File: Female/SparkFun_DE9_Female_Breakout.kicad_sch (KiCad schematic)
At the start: 9 parts, among them J2 Conn_01x09, J3 Conn_01x01, J4 Conn_01x01, J5 DB9-Female

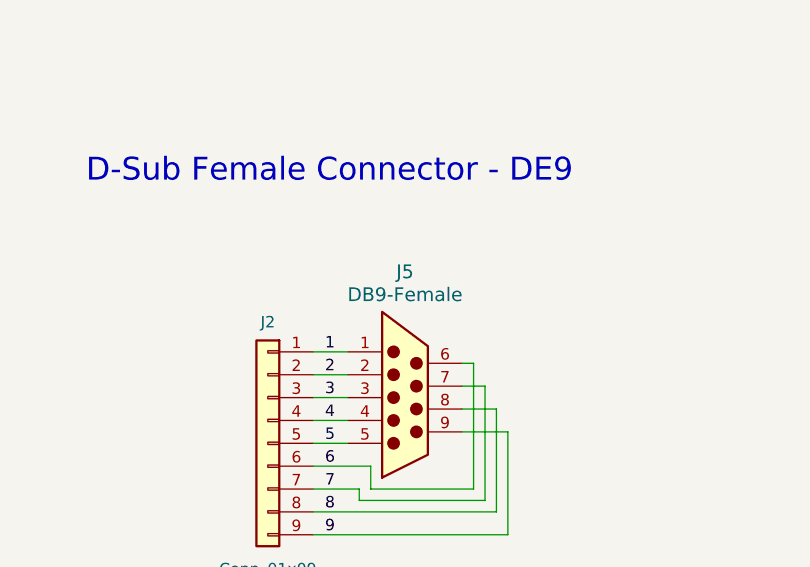
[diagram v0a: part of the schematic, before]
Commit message: Updates symbol, footprint, and design with the new renamed parts
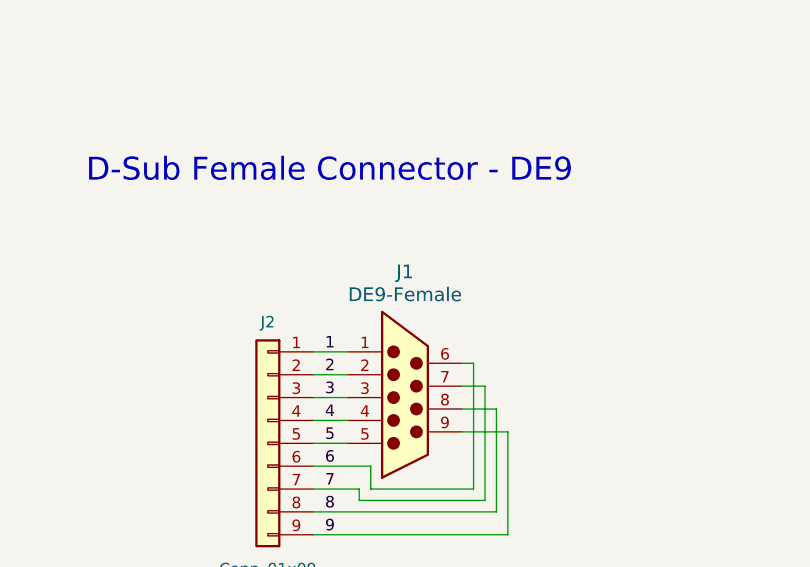
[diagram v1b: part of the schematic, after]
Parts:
- removed J5: DB9-Female, DE9_Footprint:DB9_Female, symbol DB9-Female:DB9 Female
- added J1: DE9-Female, DE9-Footprints:DE9_Female, symbol DE9-Female:DE9 Female
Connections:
- net 1: now also J1.1
- net 2: now also J1.2
- net 3: now also J1.3
- net 4: now also J1.4
- net 5: now also J1.5
- net 6: now also J1.6
- net 7: now also J1.7
- net 8: now also J1.8
- net 9: now also J1.9
